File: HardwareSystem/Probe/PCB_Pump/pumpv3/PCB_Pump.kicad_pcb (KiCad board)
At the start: 2 copper layers, 80 x 53.6 mm, 34 parts, among them J1 Conn_01x04_Pin, P1 PinHeader_1x02_P2.54mm_Vertic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, P2 PinHeader_1x02_P2.54mm_Vertic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, Q1 IRF510, Q2 IRF4905, U2 MC33063AP, U3 LM7805_TO220

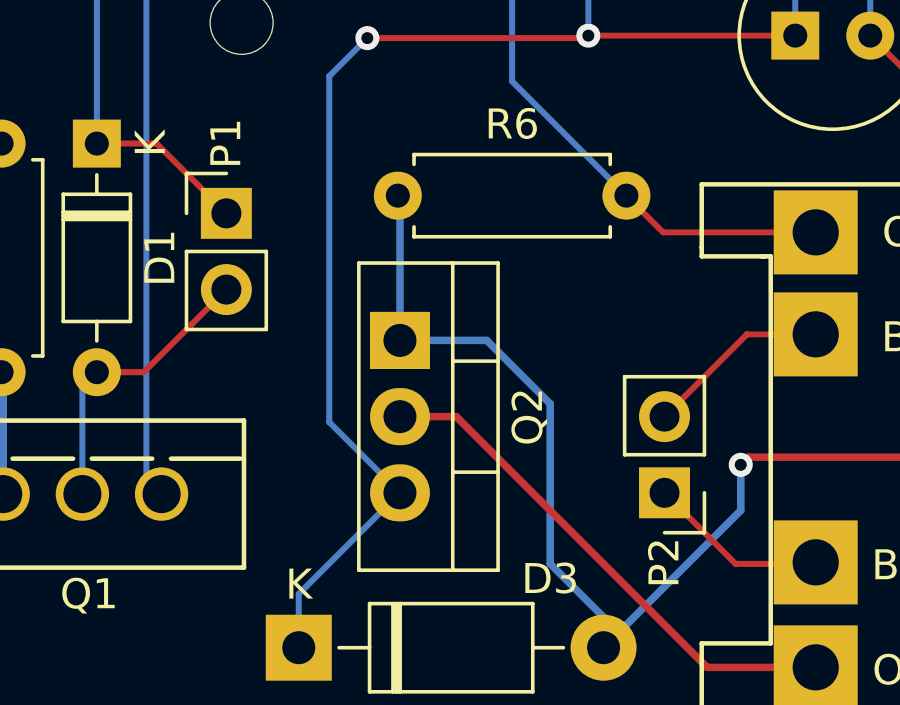
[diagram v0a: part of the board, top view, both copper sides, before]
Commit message: pumpv3-added some symbols
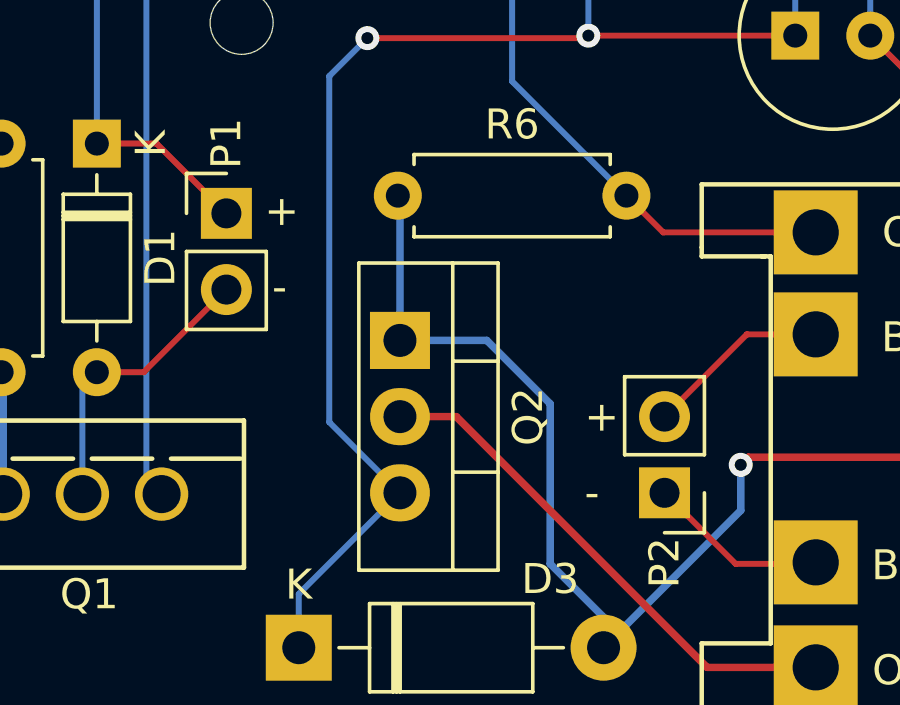
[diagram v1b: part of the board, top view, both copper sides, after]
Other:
- board text added: "+"
- board text added: "-"
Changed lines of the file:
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@@
   (gr_rect (start 84.709 42.335625) (end 164.719 95.929625)
     (stroke (width 0.1) (type default)) (fill none) (layer "Edge.Cuts"))
+  (gr_text "+" (at 121.666 74.676) (layer "F.SilkS")
+    (effects (font (size 1 1) (thickness 0.15)) (justify left bottom))
+  )
   (gr_text "APWS-SP10\nAlexis Torres, Evan LeBel, Ian Skillman,\nJaime Sanchez, Javier Padilla, Jesus Hernandez, \nKiet Le, Rodrigo Romero" (at 100.33 86.106 90) (layer "F.SilkS")
     (effects (font (size 1 1) (thickness 0.15)) (justify left bottom))
   )
+  (gr_text "+" (at 132.334 81.534) (layer "F.SilkS")
+    (effects (font (size 1 1) (thickness 0.15)) (justify left bottom))
+  )
+  (gr_text "-" (at 132.334 84.074) (layer "F.SilkS")
+    (effects (font (size 1 1) (thickness 0.15)) (justify left bottom))
+  )
+  (gr_text "-" (at 121.92 77.216) (layer "F.SilkS")
+    (effects (font (size 1 1) (thickness 0.15)) (justify left bottom))
+  )

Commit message: updates on both boards
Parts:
- added J2: Conn_01x04_Pin, Connector_PinHeader_2.54mm:PinHeader_1x04_P2.54mm_Vertical, F.Cu at (88.1, 78.7)
- moved 5V 0.76 mm to (113.3, 65.0)
- moved Q1 0.23 mm to (113.2, 83.5)
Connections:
- A2 pad A4: unconnected-(A2-A4/SDA-PadA4) -> SDA
- A2 pad A5: unconnected-(A2-A5/SCL-PadA5) -> SCL
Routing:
- net 3V7-: track 160.8 -> 194.1 mm
- net SDA: track 0.00 -> 23.3 mm
- net SCL: track 0.00 -> 23.3 mm
- net pump+: track 69.8 -> 76.2 mm
